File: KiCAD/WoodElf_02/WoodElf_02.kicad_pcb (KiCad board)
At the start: 2 copper layers, 19.2 x 19.2 mm, 19 parts

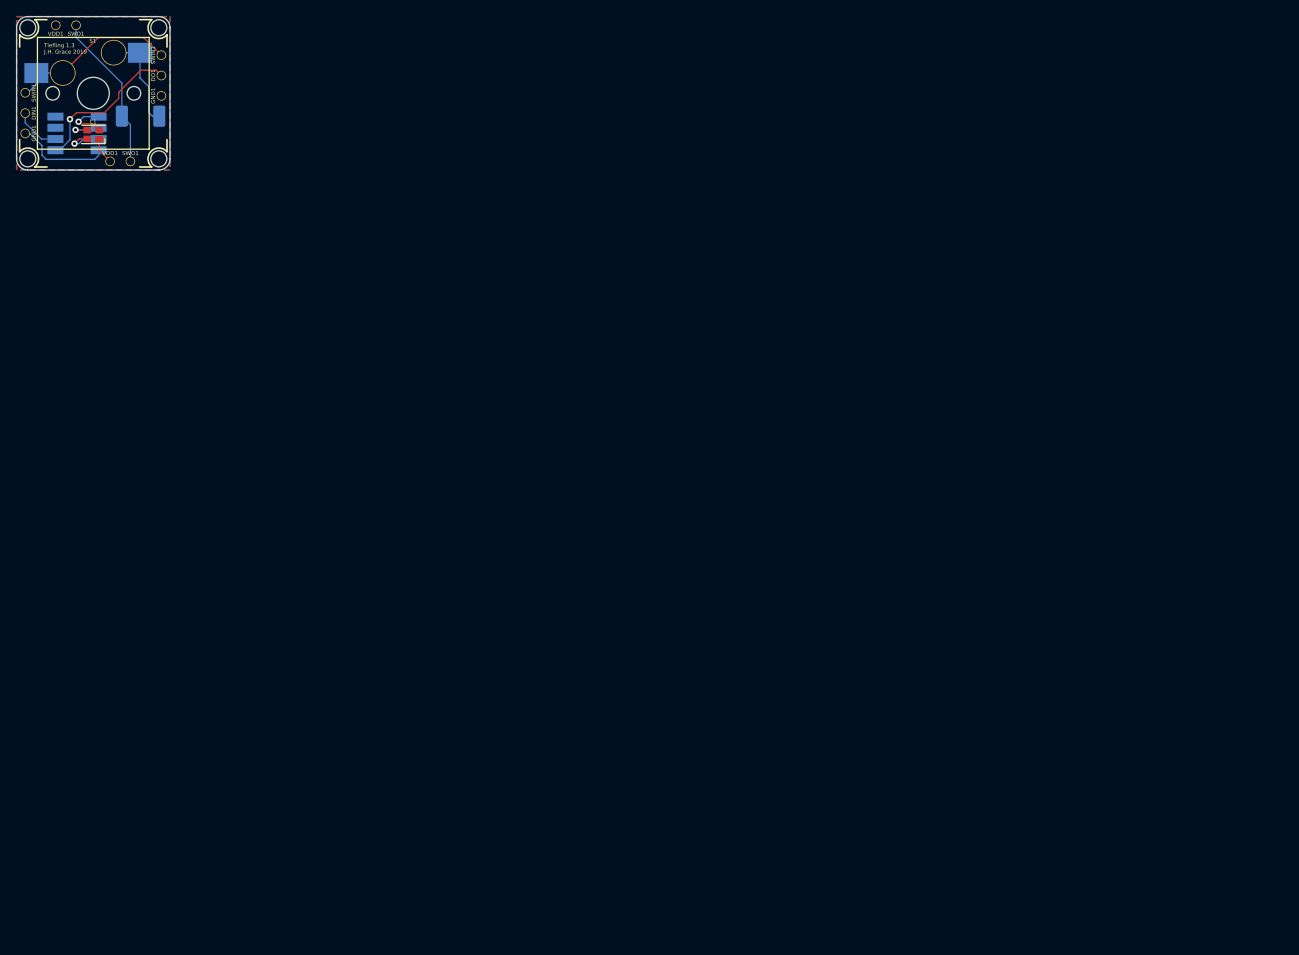
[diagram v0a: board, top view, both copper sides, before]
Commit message: droped screw sizes for pcb down from M2 to M1.6 to allow for proper sizing of array
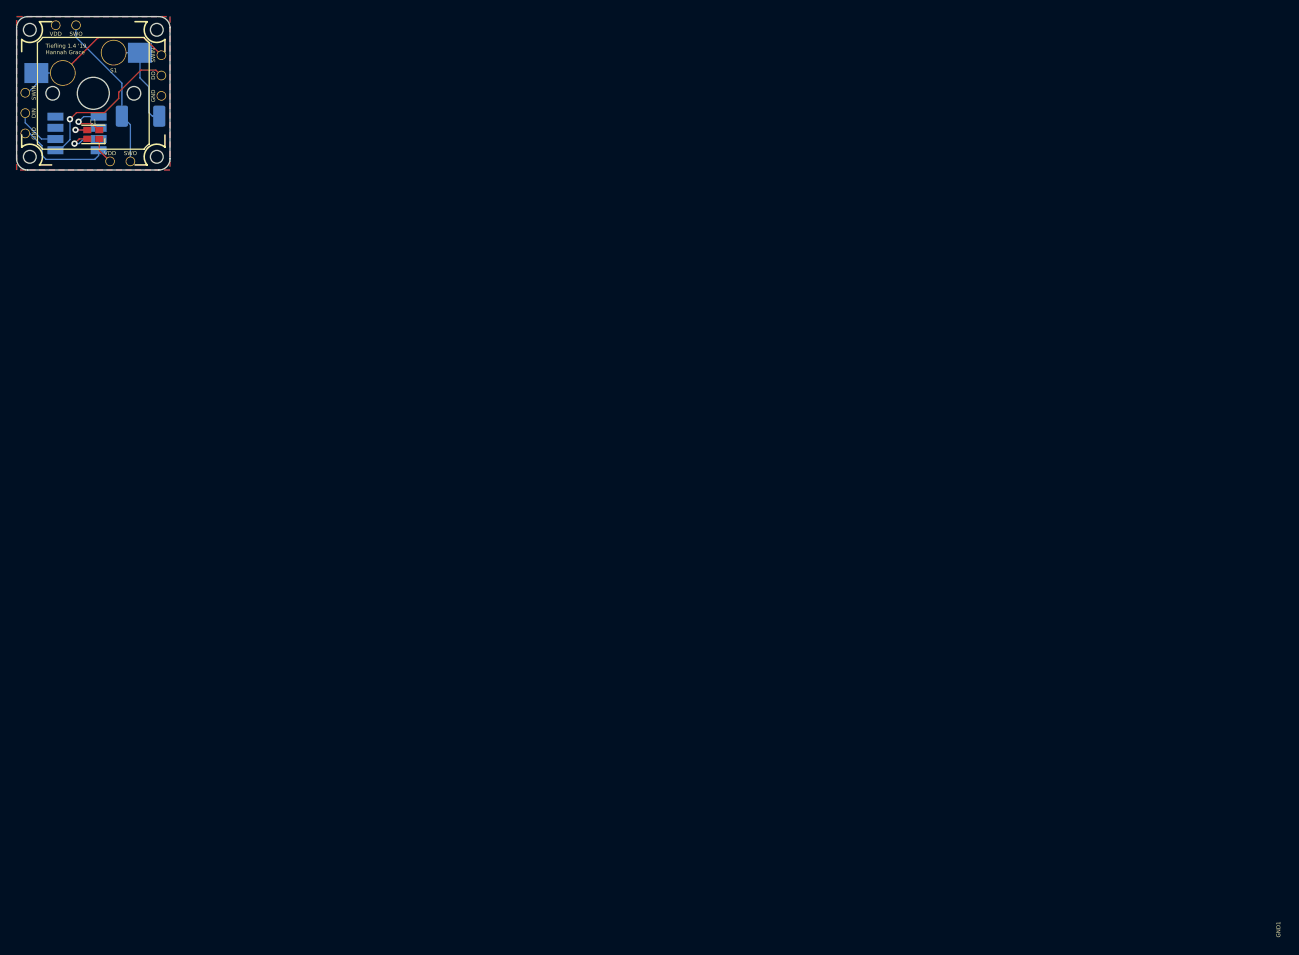
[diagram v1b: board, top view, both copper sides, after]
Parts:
- removed the Mount at (132.5, 99.4)
- removed SWIN1: BlankThrough-Hole, WoodElf_Lib:BlankThrough-Hole
- added ?: , , F.Cu at (149.0, 107.4)
- added Mount: Mount, WoodElf_Lib:Mount, F.Cu at (132.7, 99.7)
- added SWIN: BlankThrough-Hole, WoodElf_Lib:BlankThrough-Hole, F.Cu at (132.1, 107.6)
- Mount (x3): footprint WoodElfLib:Mount -> WoodElf_Lib:Mount
- moved Mount 0.36 mm to (148.6, 115.6)
- moved Mount 0.36 mm to (132.7, 115.6)
- moved Mount 0.36 mm to (148.6, 99.7)
- renumbered DIN1 to DIN, DO1 to DO, GND1 to GND, SWIN1 to SWIN, SWO1 to SWO, VDD1 to VDD
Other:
- board text added: "DIN"
- board text added: "DO"
- board text added: "GND"
- board text added: "SWIN"
- board text added: "SWO"
- board text added: "Tiefling 1.4 '19 Hannah Grace"
- board text added: "VDD"
- board text removed: "Tiefling 1.3 J.H. Grace 2019"

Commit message: Added a logo
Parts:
- removed the Mount at (148.6, 99.7)
- removed the Mount at (132.7, 99.7)
- added G***: Tiefling_Logo, WoodElf_Lib:Tiefling_Logo, F.Cu at (144.9, 111.6)
- added G***: Tiefling_LogoSmall, WoodElf_Lib:Tiefling_LogoSmall, B.Cu at (148.3, 115.4)
- added Mount: Mount, WoodElf_Lib:Mount, F.Cu at (146.0, 99.0)
- added Mount: Mount, WoodElf_Lib:Mount, F.Cu at (132.0, 102.3)
- moved Mount 2.70 mm to (135.3, 116.3), turned to 180 degrees
- moved Mount 2.70 mm to (149.3, 113.0), turned to 270 degrees
- moved D1 0.59 mm to (146.0, 110.3)
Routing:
- net /GND: track 12.1 -> 2.88 mm, vias 0 -> 1
- net Net-(C1-Pad3): track 6.48 -> 5.11 mm
- net Net-(D1-Pad1): track 13.5 -> 12.6 mm
- net /DO: track 19.6 -> 20.3 mm
- net Net-(C1-Pad2): track 4.48 -> 5.12 mm
- net Net-(C1-Pad1): track 6.16 -> 6.76 mm
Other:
- outline, holes or cut-outs redrawn
- board text added: "Tiefling Hannah Grace 1.4 '19"

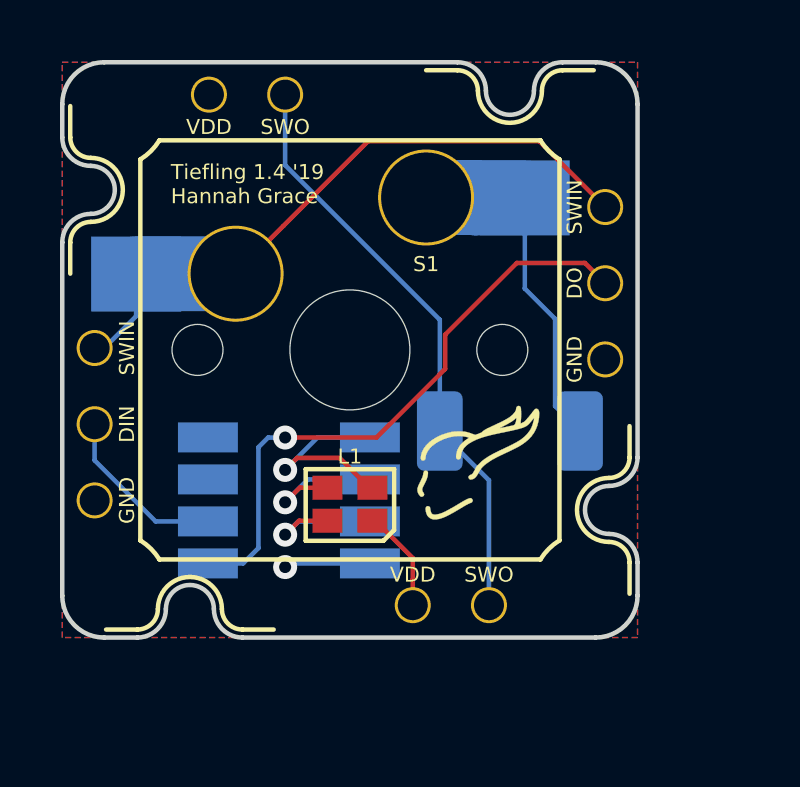
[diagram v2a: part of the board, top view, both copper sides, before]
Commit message: got rid of the tiny LED and replaced with an SK6812MINI
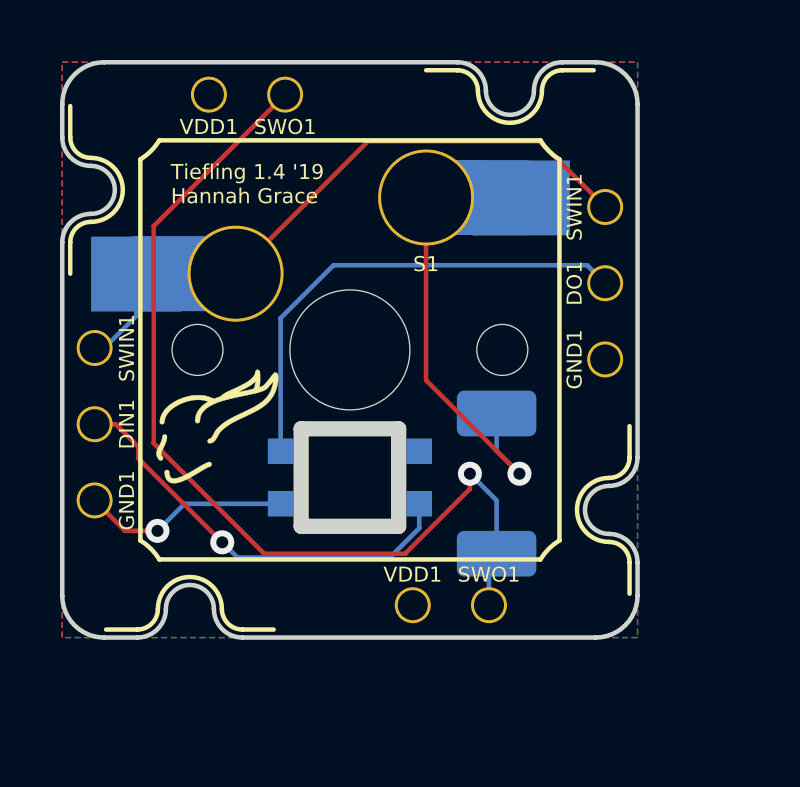
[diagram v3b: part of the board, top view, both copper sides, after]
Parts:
- removed C1: WS2811, WoodElf_Lib:WS2811
- L1: value LED_ARGB -> SK6812MINI; footprint LED_SMD:LED_Cree-PLCC4_2x2mm_CW -> WoodElf_Lib:LED_SK6812MINI_PLCC4_3.5x3.5mm_P1.75mm
- moved G*** 12.7 mm to (137.2, 109.2), turned to 270 degrees
- moved G 8.78 mm to (136.2, 110.4)
- moved D1 1.81 mm to (145.5, 112.1), turned to 270 degrees
- moved L1 0.89 mm to (140.7, 111.9), turned to 0 degrees
- renumbered DIN to DIN1, DO to DO1, G*** to G, GND to GND1, SWIN to SWIN1, SWO to SWO1, VDD to VDD1
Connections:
- L1 pad 1: /USB -> /DO
- L1 pad 2: Net-(C1-Pad3) -> /GND
- L1 pad 3: Net-(C1-Pad2) -> /DIN
- L1 pad 4: Net-(C1-Pad1) -> /USB
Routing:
- net /SWO: track 19.8 -> 31.8 mm, vias 0 -> 1
- net /DIN: track 5.83 -> 14.1 mm, vias 0 -> 1
- net Net-(C1-Pad1): track 6.76 -> 0.00 mm, vias 1 -> 0
- net Net-(C1-Pad2): track 5.12 -> 0.00 mm, vias 1 -> 0
- net Net-(C1-Pad3): track 5.11 -> 0.00 mm, vias 1 -> 0
- net /GND: track 2.88 -> 7.15 mm
- net /DO: track 20.3 -> 16.2 mm, vias 1 -> 0
- net Net-(D1-Pad1): track 12.6 -> 16.1 mm, vias 0 -> 1
- net /USB: track 3.53 -> 0.00 mm
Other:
- outline, holes or cut-outs redrawn

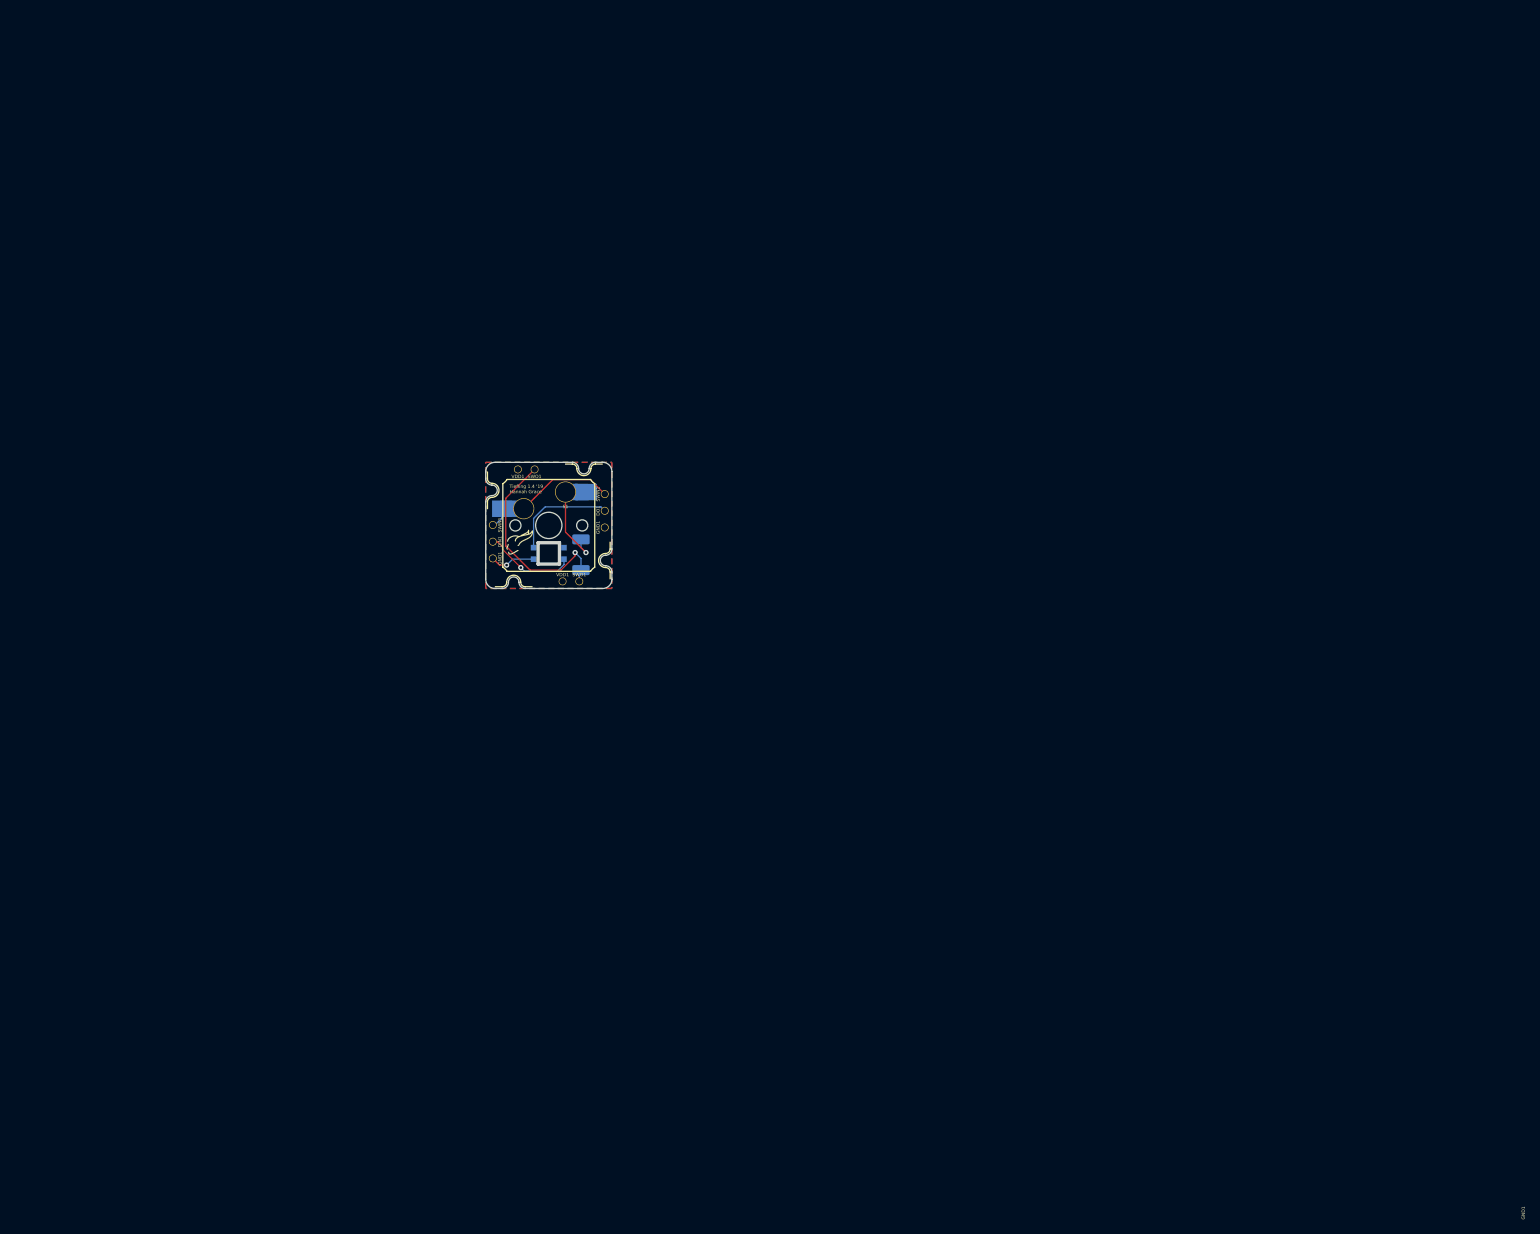
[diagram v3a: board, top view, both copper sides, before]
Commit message: Started on the Joystick breakout plate
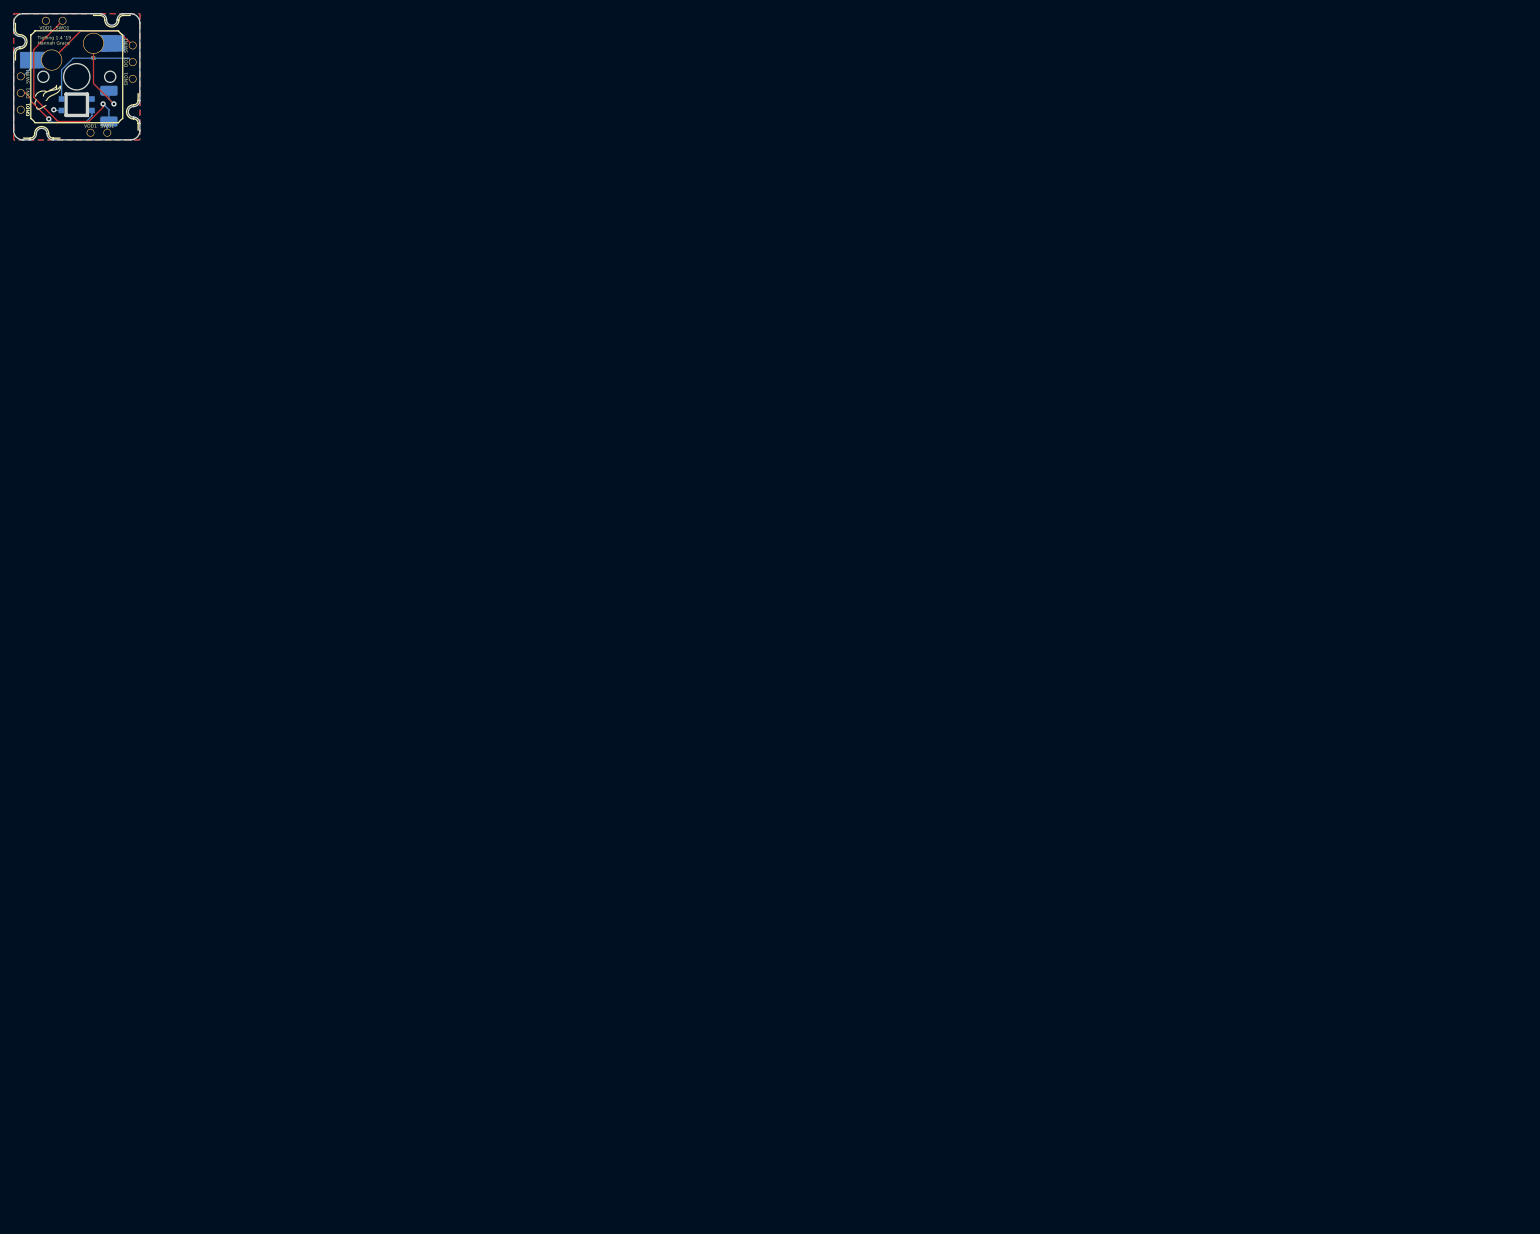
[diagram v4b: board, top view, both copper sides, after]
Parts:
- moved GND1 99.0 mm to (77.4, 39.8)
- moved H1 99.0 mm to (71.4, 34.4)
- moved Mount 99.0 mm to (60.3, 34.1)
- moved Mount 99.0 mm to (63.6, 48.1)
- moved SWIN1 99.0 mm to (77.4, 34.7)
- moved SWIN1 99.0 mm to (60.4, 39.4)
- moved SWO1 99.0 mm to (66.7, 30.9)
- moved VDD1 99.0 mm to (64.2, 30.9)
- moved ? 99.0 mm to (77.2, 39.2)
- moved L1 99.0 mm to (68.9, 43.7)
- moved Mount 99.0 mm to (74.2, 30.8)
- moved SWO1 99.0 mm to (73.5, 47.9)
- moved D1 99.0 mm to (73.8, 43.9)
- moved DIN1 99.0 mm to (60.4, 41.9)
- moved DO1 99.0 mm to (77.4, 37.2)
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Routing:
- net /GND: track 7.15 -> 1.39 mm

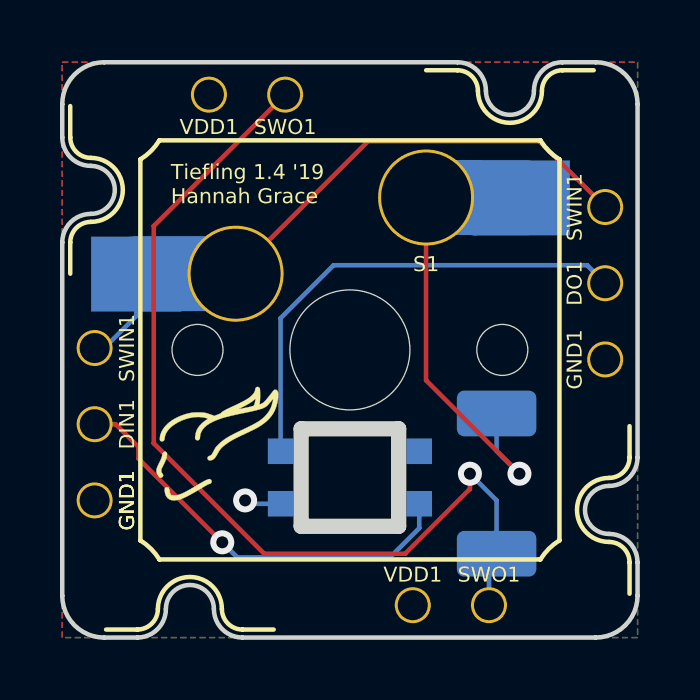
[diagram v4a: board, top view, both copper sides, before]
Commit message: reworked the outer edge of the PCB
turns out i didnt consider how the tiling screw holes would fit with the wire holes - it should all be good now and not interfere with itself
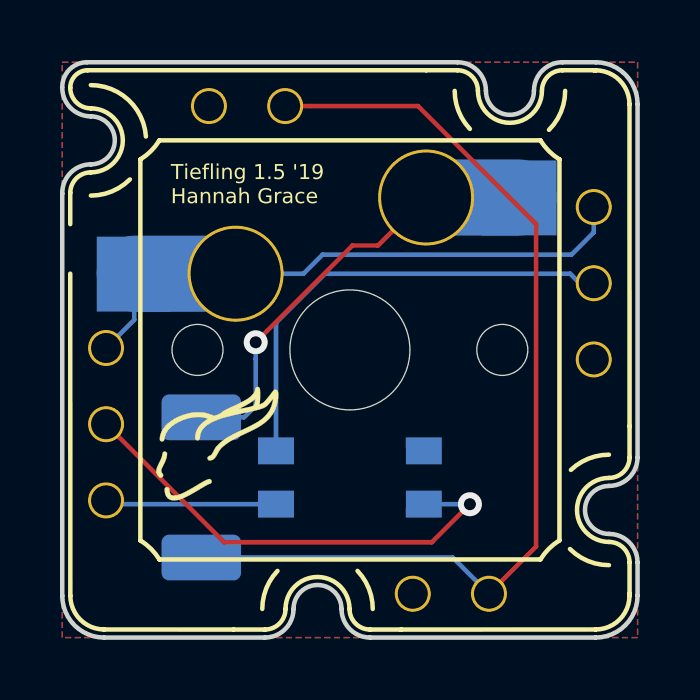
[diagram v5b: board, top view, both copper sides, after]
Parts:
- moved LOGOsmll 12.1 mm to (75.8, 47.3)
- moved D1 9.84 mm to (63.9, 44.0)
- moved Mount 4.25 mm to (67.8, 48.1)
- moved Mount 1.65 mm to (60.3, 32.4)
- moved DIN1 0.38 mm to (60.8, 41.9)
- moved DO1 0.38 mm to (77.0, 37.2)
- moved GND1 0.38 mm to (77.0, 39.8)
- moved GND1 0.38 mm to (60.8, 44.5)
- moved SWIN1 0.38 mm to (77.0, 34.7)
- moved SWIN1 0.38 mm to (60.8, 39.4)
- moved SWO1 0.38 mm to (73.5, 47.6)
- moved SWO1 0.38 mm to (66.7, 31.3)
- moved VDD1 0.38 mm to (71.0, 47.6)
- moved VDD1 0.38 mm to (64.2, 31.3)
- renumbered G*** to LOGOsmll
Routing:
- net /GND: track 1.39 -> 6.06 mm, vias 1 -> 0
- net /DIN: track 14.1 -> 15.9 mm
- net /SWO: track 31.8 -> 33.1 mm, vias 1 -> 0
- net Net-(D1-Pad1): track 16.1 -> 14.9 mm
- net /DO: track 16.2 -> 15.7 mm
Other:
- outline, holes or cut-outs redrawn
- board text added: "Tiefling 1.5 '19 Hannah Grace"
- board text removed: "Tiefling 1.4 '19 Hannah Grace"
- board text removed: "Tiefling Hannah Grace 1.4 '19"
